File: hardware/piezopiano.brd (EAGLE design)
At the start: 90 x 99.8 mm, 112 parts, among them J2 CON2, Q1 DMN3404L, Q2 DMN3404L, Q3 DMN3404L, Q4 DMN3404L, Q5 DMN3404L, Q6 DMN3404L, Q7 DMN3404L, Q8 DMN3404L, Q9 DNP, U1 CH340E_MSOP10, U2 ATMEGA4809, U3 DNP

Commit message: Routed RST
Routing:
- net RESETN: track 0.00 -> 71.2 mm, vias 0 -> 4
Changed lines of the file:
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@@
 <drawing>
 <settings>
-<setting alwaysvectorfont="yes"/>
+<setting alwaysvectorfont="no"/>
 <setting verticaltext="up"/>
 </settings>
@@
 <contactref element="U2" pad="40"/>
 <contactref element="C17" pad="2"/>
-<wire x1="34.9067625" y1="25.638996875" x2="25.75" y2="90.25" width="0" layer="19" extent="1-1"/>
+<wire x1="34.9067625" y1="25.638996875" x2="34.258884375" y2="24.99111875" width="0.254" layer="1"/>
+<via x="34.258884375" y="24.99111875" extent="1-16" drill="0.3"/>
+<wire x1="34.258884375" y1="24.99111875" x2="33.50888125" y2="24.99111875" width="0.254" layer="16"/>
+<wire x1="33.50888125" y1="24.99111875" x2="31.5" y2="27" width="0.254" layer="16"/>
+<wire x1="25.75" y1="90.25" x2="25" y2="90.25" width="0.254" layer="1"/>
+<via x="25" y="90.25" extent="1-16" drill="0.3"/>
+<wire x1="25" y1="90.25" x2="25" y2="76" width="0.254" layer="16"/>
+<wire x1="25" y1="76" x2="25.5" y2="75.5" width="0.254" layer="16"/>
+<via x="25.5" y="75.5" extent="1-16" drill="0.3"/>
+<wire x1="31.5" y1="40" x2="27" y2="44.5" width="0.254" layer="16"/>
+<via x="27" y="44.5" extent="1-16" drill="0.3"/>
+<wire x1="27" y1="44.5" x2="25.5" y2="46" width="0.254" layer="1"/>
+<wire x1="25.5" y1="46" x2="25.5" y2="75.5" width="0.254" layer="1"/>
+<wire x1="31.5" y1="27" x2="31.5" y2="40" width="0.254" layer="16"/>
 </signal>
 <signal name="D3~">

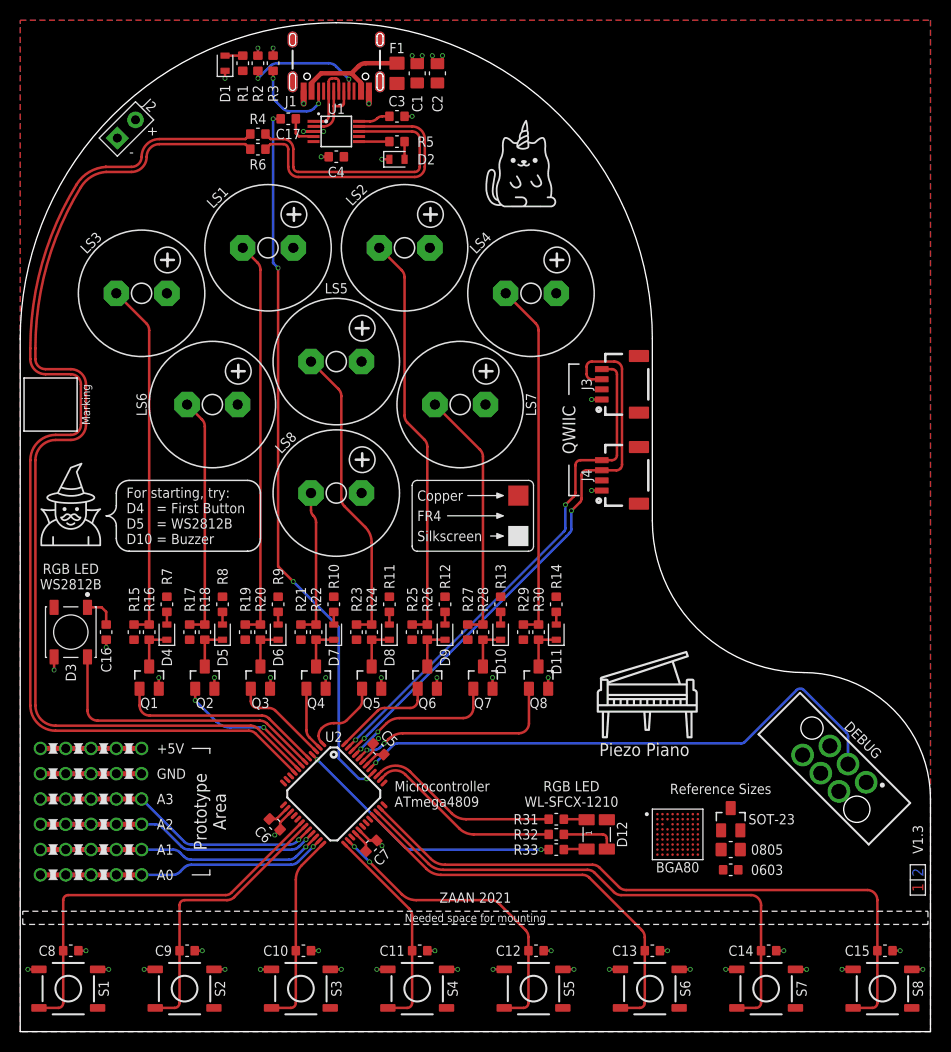
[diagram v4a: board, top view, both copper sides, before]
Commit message: Added diode, renamed pins to pinout
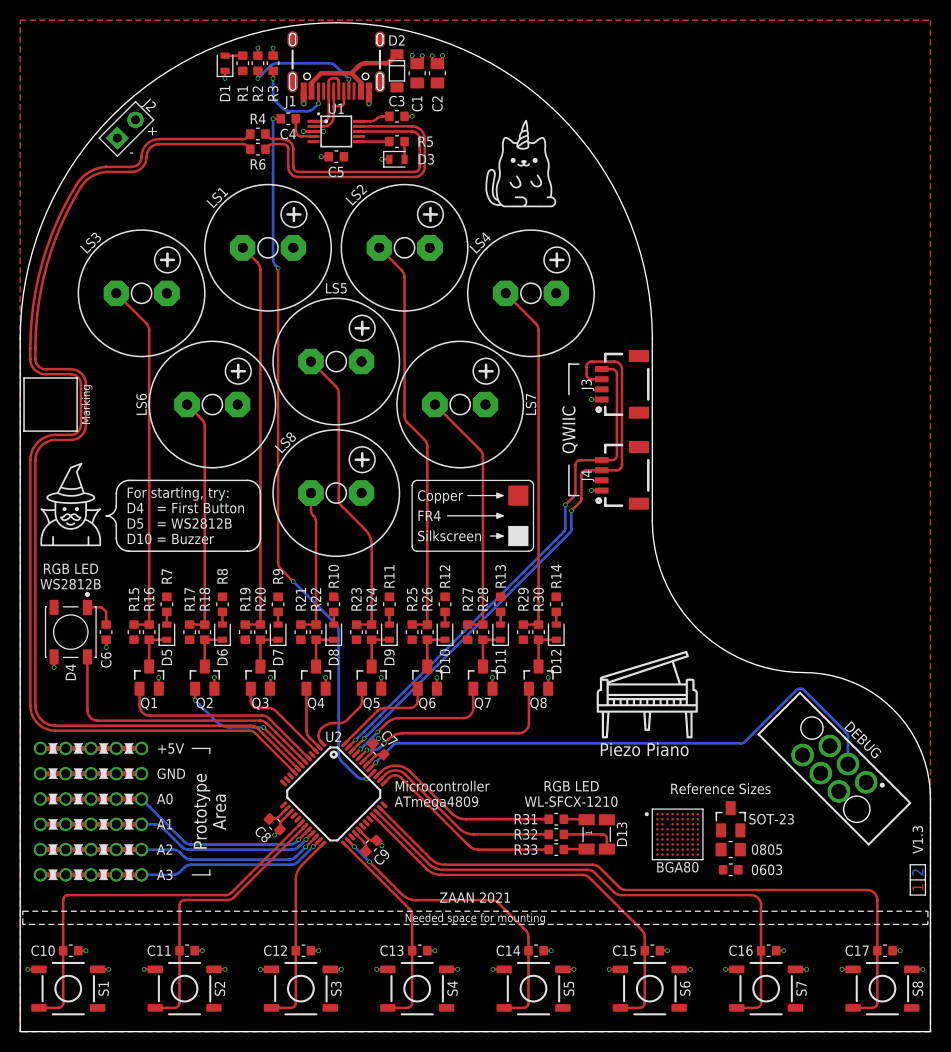
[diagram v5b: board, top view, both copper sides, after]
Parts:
- removed F1: MF-PSMF035X-2, zaan-Fuses:F0805
- added D13: (no value), zaan-Optoelectronics:WL-SFCX_1210
- D12: value (none) -> LED_YELLOW; device zaan-Optoelectronics:WL-SFCX_1210 -> zaan-Optoelectronics:LEDC1608X55N_FLAT-Y
- D2: value LED_YELLOW -> B5819WSL; device zaan-Optoelectronics:LEDC1608X55N_FLAT-Y -> zaan-Discrete:SOD123
- D3: value WS2812B -> LED_YELLOW; device zaan-Optoelectronics:WS2812B -> zaan-Optoelectronics:LEDC1608X55N_FLAT-Y
- D4: value LED_YELLOW -> WS2812B; device zaan-Optoelectronics:LEDC1608X55N_FLAT-Y -> zaan-Optoelectronics:WS2812B
- moved C17 101.2 mm to (85.5, 8.00), turned to 0 degrees
- moved C16 72.7 mm to (74.0, 8.00), turned to 0 degrees
- moved C5 58.7 mm to (31.2, 86.5), turned to 180 degrees
- moved D3 56.8 mm to (37.2, 86.2), turned to 0 degrees
- moved C6 25.3 mm to (8.50, 39.5), turned to 270 degrees
- moved C8 23.7 mm to (25.2, 20.5), turned to 315 degrees
- moved C10 23.0 mm to (5.00, 8.00)
- moved C11 23.0 mm to (16.5, 8.00)
- moved C12 23.0 mm to (28.0, 8.00)
- moved C13 23.0 mm to (39.5, 8.00)
- moved C14 23.0 mm to (51.0, 8.00)
- moved C15 23.0 mm to (62.5, 8.00)
- moved C9 21.0 mm to (34.7, 18.4), turned to 45 degrees
- moved D12 20.4 mm to (53.0, 39.5), turned to 90 degrees
- moved C7 9.57 mm to (35.4, 27.9), turned to 135 degrees
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- renumbered U$8 to U$3
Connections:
- net A0 renamed D25/A3
- net A1 renamed D24/A2
- net A2 renamed D23/A1
- net A3 renamed D22/A0
- net A4/SDA renamed D2/SDA
- net A5/SCL renamed D3/SCL
- net AREF renamed D29/A7/AREF
- net D10~ renamed D9
- net D2 renamed D0
- net D3~ renamed D39~/A15
- net D6~ renamed D38~/A14
- net MISO renamed D31/A9
- net MOSI renamed D30/A8
- net PA05 renamed D5
- net PA06 renamed D6
- net PB03 renamed D11
- net PC00 renamed D14~
- net PC01 renamed D15~
- net PC02 renamed D16~
- net PC03 renamed D17~
- net PF02 renamed D36/A12
- net RX0 renamed D13~/RX3
- net RX1 renamed D19~
- net SCK renamed D32/A10
- net TX0 renamed D12/TX3
- net TX1 renamed D18~
- net UDPI renamed UPDI
- removed net A6: C10.1, S3.1, S3.2, U2.24
- removed net A7: C11.1, S4.1, S4.2, U2.25
- removed net D5~: D3.4, U2.6
- removed net D9~: R33.1, U2.4
- removed net PA04: Q6.1, U2.48
- removed net PA07: Q3.1, U2.3
- removed net PC07: C9.1, S2.1, S2.2, U2.19
- removed net PD06: C12.1, S5.1, S5.2, U2.26
- removed net PF00: C14.1, S7.1, S7.2, U2.34
- removed net PF01: C15.1, S8.1, S8.2, U2.35
- removed net PF03: U2.37
- new net D1: Q7.1, U2.45
- new net D10: D4.4, U2.6
- new net D20: C10.1, S1.1, S1.2, U2.18
- new net D21: C11.1, S2.1, S2.2, U2.19
- new net D26/A4: C12.1, S3.1, S3.2, U2.24
- new net D27/A5: C13.1, S4.1, S4.2, U2.25
- new net D28/A6: C14.1, S5.1, S5.2, U2.26
- new net D33/A11: C15.1, S6.1, S6.2, U2.33
- new net D34: C16.1, S7.1, S7.2, U2.34
- new net D35: C17.1, S8.1, S8.2, U2.35
- new net D37/A13: R33.1, U2.37
- net +5V: now also C8.1, C9.1, D13.4, D2.A, D4.1; no longer C16.1, C4.1, D12.4, D3.1, F1.2
- net D4: now also Q6.1, U2.48; no longer C8.1, S1.1, S1.2, U2.18
- net D7: now also Q3.1, U2.3; no longer Q7.1, U2.45
- net D8: now also U2.4; no longer C13.1, S6.1, S6.2, U2.33
- net GND: now also C17.2, D3.C, D4.3; no longer C4.2, D2.C, D3.3
- net N$1: now also C4.1; no longer C17.1
- net N$12: now also D6.C; no longer D5.C
- net N$14: now also D10.C; no longer D9.C
- net N$17: now also D11.C; no longer D10.C
- net N$2: now also D8.C; no longer D7.C
- net N$20: now also D3.A; no longer D2.A
- net N$22: now also D7.A; no longer D6.A
- net N$23: now also D9.A; no longer D8.A
- net N$24: now also D10.A; no longer D9.A
- net N$25: now also D8.A; no longer D7.A
- net N$26: now also D12.A; no longer D11.A
- net N$27: now also D5.A; no longer D4.A
- net N$28: now also D13.1; no longer D12.1
- net N$3: now also D5.C; no longer D4.C
- net N$33: now also D6.A; no longer D5.A
- net N$34: now also D11.A; no longer D10.A
- net N$35: now also D13.2; no longer D12.2
- net N$36: now also D13.3; no longer D12.3
- net N$5: now also D9.C; no longer D8.C
- net N$7: now also D12.C; no longer D11.C
- net N$9: now also D7.C; no longer D6.C
- net RESETN: now also C4.2; no longer C17.2
- net VBUS: now also D2.C; no longer F1.1
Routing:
- net PF01: track 65.4 -> 0.00 mm
- net D35: track 0.00 -> 65.4 mm
- net PF00: track 53.8 -> 0.00 mm
- net D34: track 0.00 -> 53.8 mm
- net D8: track 40.9 -> 0.00 mm
- net D33/A11: track 0.00 -> 40.9 mm
- net D20: track 0.00 -> 39.4 mm
- net D28/A6: track 0.00 -> 30.9 mm, vias 0 -> 2
- net PD06: track 30.9 -> 0.00 mm, vias 2 -> 0
- net D4: track 39.4 -> 10.1 mm
- net D5~: track 28.8 -> 0.00 mm
- net D10: track 0.00 -> 28.8 mm
- net PC07: track 27.8 -> 0.00 mm
- net D21: track 0.00 -> 27.8 mm
- net D9~: track 27.2 -> 0.00 mm, vias 2 -> 0
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
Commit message: Pinout change piezos, silkscreen edit
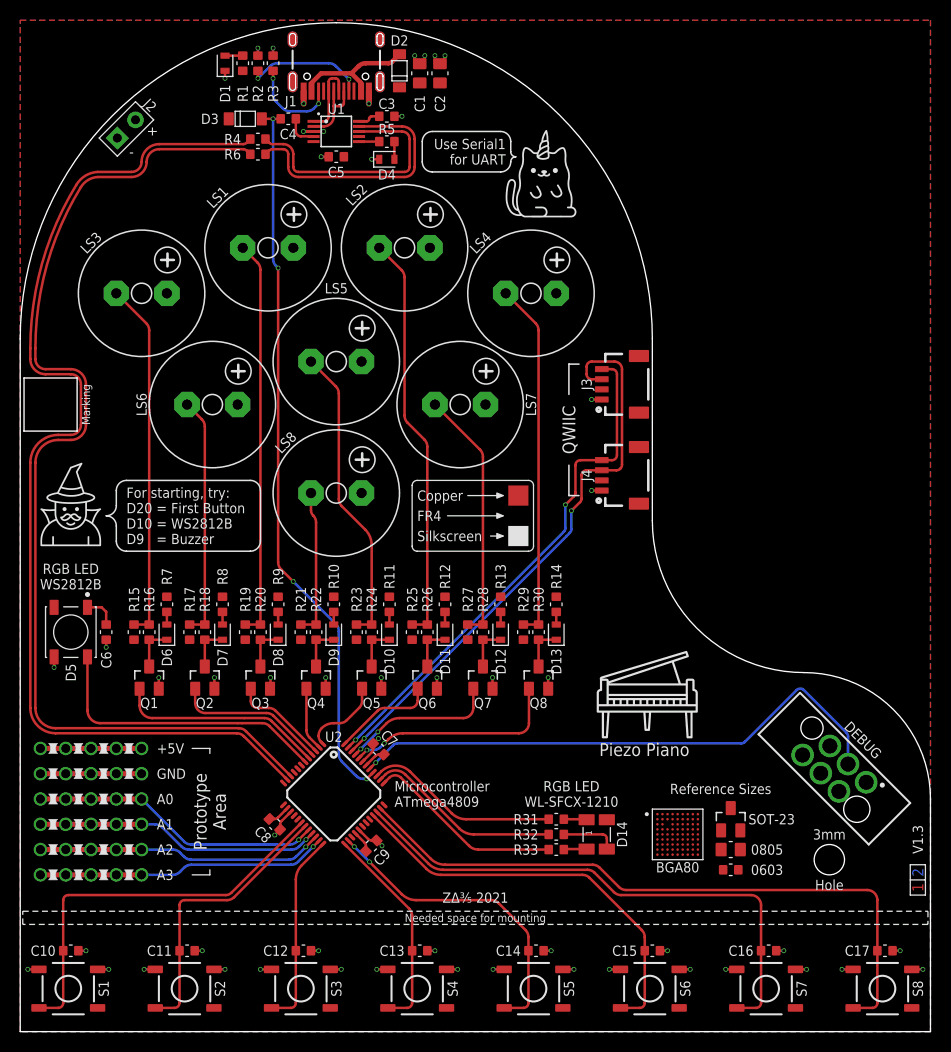
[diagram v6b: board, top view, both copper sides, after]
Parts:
- added D14: (no value), zaan-Optoelectronics:WL-SFCX_1210
- D13: value (none) -> LED_YELLOW; device zaan-Optoelectronics:WL-SFCX_1210 -> zaan-Optoelectronics:LEDC1608X55N_FLAT-Y
- D3: value LED_YELLOW -> B5819WSL; device zaan-Optoelectronics:LEDC1608X55N_FLAT-Y -> zaan-Discrete:SOD123
- D4: value WS2812B -> LED_YELLOW; device zaan-Optoelectronics:WS2812B -> zaan-Optoelectronics:LEDC1608X55N_FLAT-Y
- D5: value LED_YELLOW -> WS2812B; device zaan-Optoelectronics:LEDC1608X55N_FLAT-Y -> zaan-Optoelectronics:WS2812B
- moved D4 56.2 mm to (36.2, 86.2), turned to 0 degrees
- moved D13 20.4 mm to (53.0, 39.5), turned to 90 degrees
- moved D3 15.5 mm to (22.2, 90.2)
- moved D5 9.50 mm to (5.00, 39.5), turned to 270 degrees
- moved D10 5.50 mm to (36.5, 39.5)
- moved D11 5.50 mm to (42.0, 39.5)
- moved D12 5.50 mm to (47.5, 39.5)
- moved D6 5.50 mm to (14.5, 39.5)
- moved D7 5.50 mm to (20.0, 39.5)
- moved D8 5.50 mm to (25.5, 39.5)
- moved D9 5.50 mm to (31.0, 39.5)
- moved U$1 2.24 mm to (48.0, 80.5)
- moved C3 1.00 mm to (36.2, 90.5)
- moved R5 1.00 mm to (36.2, 88.0)
- moved R4 0.50 mm to (23.5, 88.2)
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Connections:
- removed net D12/TX3: R6.1, U2.8
- removed net D13~/RX3: R4.1, U2.9
- removed net D14~: U2.10
- removed net D15~: U2.11
- new net D12: U2.8
- new net D13~: U2.9
- new net D14~/TX1: R6.1, U2.10
- new net D15~/RX1: R4.1, U2.11
- net +5V: now also D14.4, D2.C, D3.C, D5.1; no longer D13.4, D2.A, D4.1
- net D10: now also D5.4; no longer D4.4
- net D11: no longer Q2.1
- net D8: now also Q2.1
- net GND: now also D4.C, D5.3; no longer D3.C, D4.3
- net N$12: now also D7.C; no longer D6.C
- net N$14: now also D11.C; no longer D10.C
- net N$17: now also D12.C; no longer D11.C
- net N$2: now also D9.C; no longer D8.C
- net N$20: now also D4.A; no longer D3.A
- net N$22: now also D8.A; no longer D7.A
- net N$23: now also D10.A; no longer D9.A
- net N$24: now also D11.A; no longer D10.A
- net N$25: now also D9.A; no longer D8.A
- net N$26: now also D13.A; no longer D12.A
- net N$27: now also D6.A; no longer D5.A
- net N$28: now also D14.1; no longer D13.1
- net N$3: now also D6.C; no longer D5.C
- net N$33: now also D7.A; no longer D6.A
- net N$34: now also D12.A; no longer D11.A
- net N$35: now also D14.2; no longer D13.2
- net N$36: now also D14.3; no longer D13.3
- net N$5: now also D10.C; no longer D9.C
- net N$7: now also D13.C; no longer D12.C
- net N$9: now also D8.C; no longer D7.C
- net RESETN: now also D3.A
- net VBUS: now also D2.A; no longer D2.C
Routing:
- net D13~/RX3: track 106.4 -> 0.00 mm
- net D15~/RX1: track 0.00 -> 105.8 mm
- net D12/TX3: track 105.3 -> 0.00 mm
- net D14~/TX1: track 0.00 -> 104.8 mm
- net D8: track 0.00 -> 15.0 mm
- net D11: track 14.2 -> 0.00 mm, vias 2 -> 0
- net TXD: track 27.1 -> 24.6 mm
- net RXD: track 28.5 -> 26.0 mm
- net RESETN: track 70.9 -> 72.0 mm
- net N$19: track 3.00 -> 2.00 mm
- net V3: track 3.10 -> 2.21 mm
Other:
- board text added: "3mm"
- board text added: "For starting, try: D20 = First Button D10 = WS2812B D9 = Buzzer"
- board text added: "Hole"
- board text added: "Use Serial1 for UART"
- board text added: "ZΔ⅗ 2021"
- board text removed: "For starting, try: D4 = First Button D5 = WS2812B D10 = Buzzer"
- board text removed: "ZAAN 2021"

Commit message: Added caps for I2C
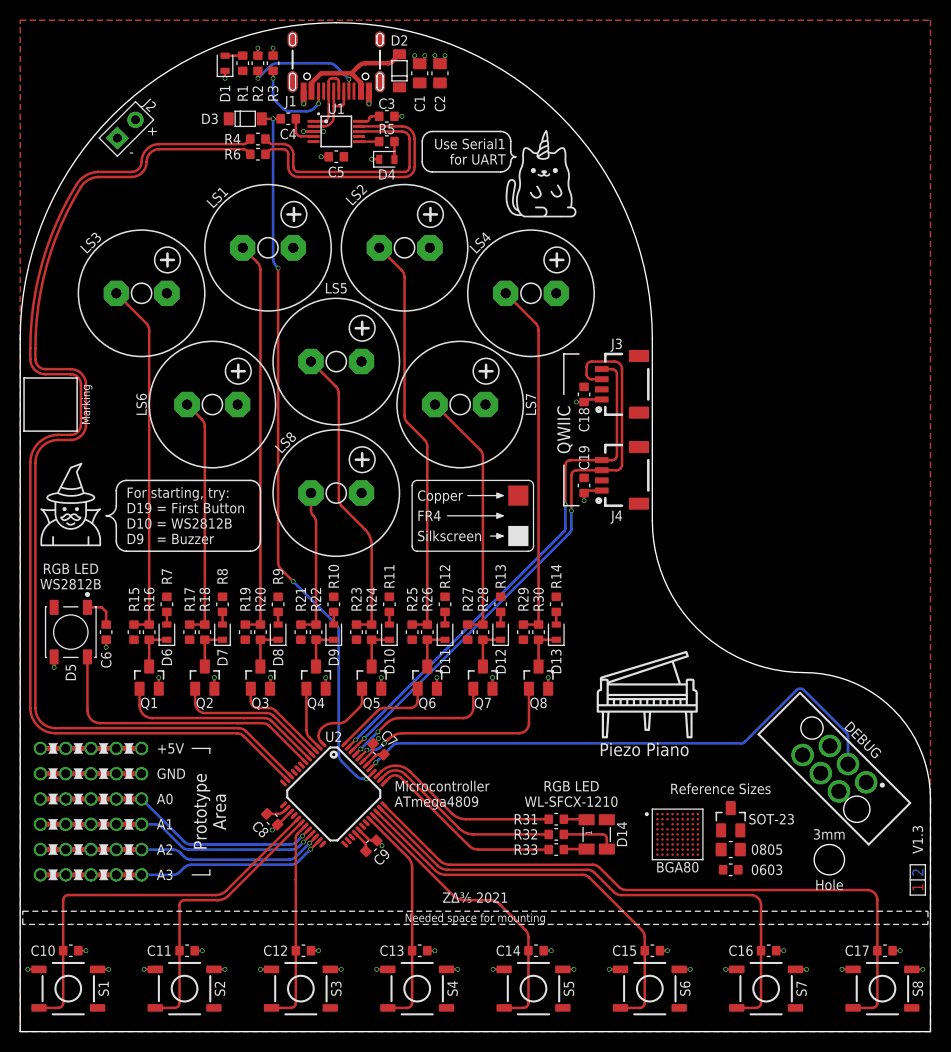
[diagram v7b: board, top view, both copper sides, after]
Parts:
- added C18, C19: 100n, zaan-Capacitors:C0603
- moved C8 0.56 mm to (24.9, 21.0)
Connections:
- net +5V: now also C18.1, C19.1
- net D19~: now also C10.1, S1.1, S1.2
- net D20: now also C11.1, S2.1, S2.2; no longer C10.1, S1.1, S1.2
- net D21: now also C12.1, S3.1, S3.2; no longer C11.1, S2.1, S2.2
- net D26/A4: no longer C12.1, S3.1, S3.2
- net D27/A5: no longer C13.1, S4.1, S4.2
- net D28/A6: no longer C14.1, S5.1, S5.2
- net D32/A10: now also C13.1, S4.1, S4.2
- net D33/A11: now also C14.1, S5.1, S5.2; no longer C15.1, S6.1, S6.2
- net D34: now also C15.1, S6.1, S6.2; no longer C16.1, S7.1, S7.2
- net D35: now also C16.1, S7.1, S7.2; no longer C17.1, S8.1, S8.2
- net D36/A12: now also C17.1, S8.1, S8.2
- net GND: now also C18.2, C19.2
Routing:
- net D36/A12: track 0.00 -> 65.2 mm
- net D19~: track 0.00 -> 39.2 mm
- net D28/A6: track 30.9 -> 0.00 mm, vias 2 -> 0
- net D32/A10: track 0.00 -> 22.4 mm
- net D27/A5: track 21.0 -> 0.00 mm
- net D26/A4: track 19.3 -> 0.00 mm
- net D34: track 53.8 -> 40.7 mm
- net D20: track 39.4 -> 27.6 mm
- net D35: track 65.4 -> 53.6 mm
- net D33/A11: track 40.9 -> 29.4 mm
- net D21: track 27.8 -> 20.4 mm
- net GND: track 58.3 -> 61.3 mm
- net D3/SCL: track 51.4 -> 52.0 mm
- net D2/SDA: track 57.0 -> 57.6 mm
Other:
- board text added: "For starting, try: D19 = First Button D10 = WS2812B D9 = Buzzer"
- board text removed: "For starting, try: D20 = First Button D10 = WS2812B D9 = Buzzer"
